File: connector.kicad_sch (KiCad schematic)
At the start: 19 parts, among them IC401 TLP185xSE, IC403 ACS71240, IC410 TLP185xSE, J400 XT60-Angled-F, Q401 HSBA8119, Q402 HSBA8119, U404 ADS1115IDGS

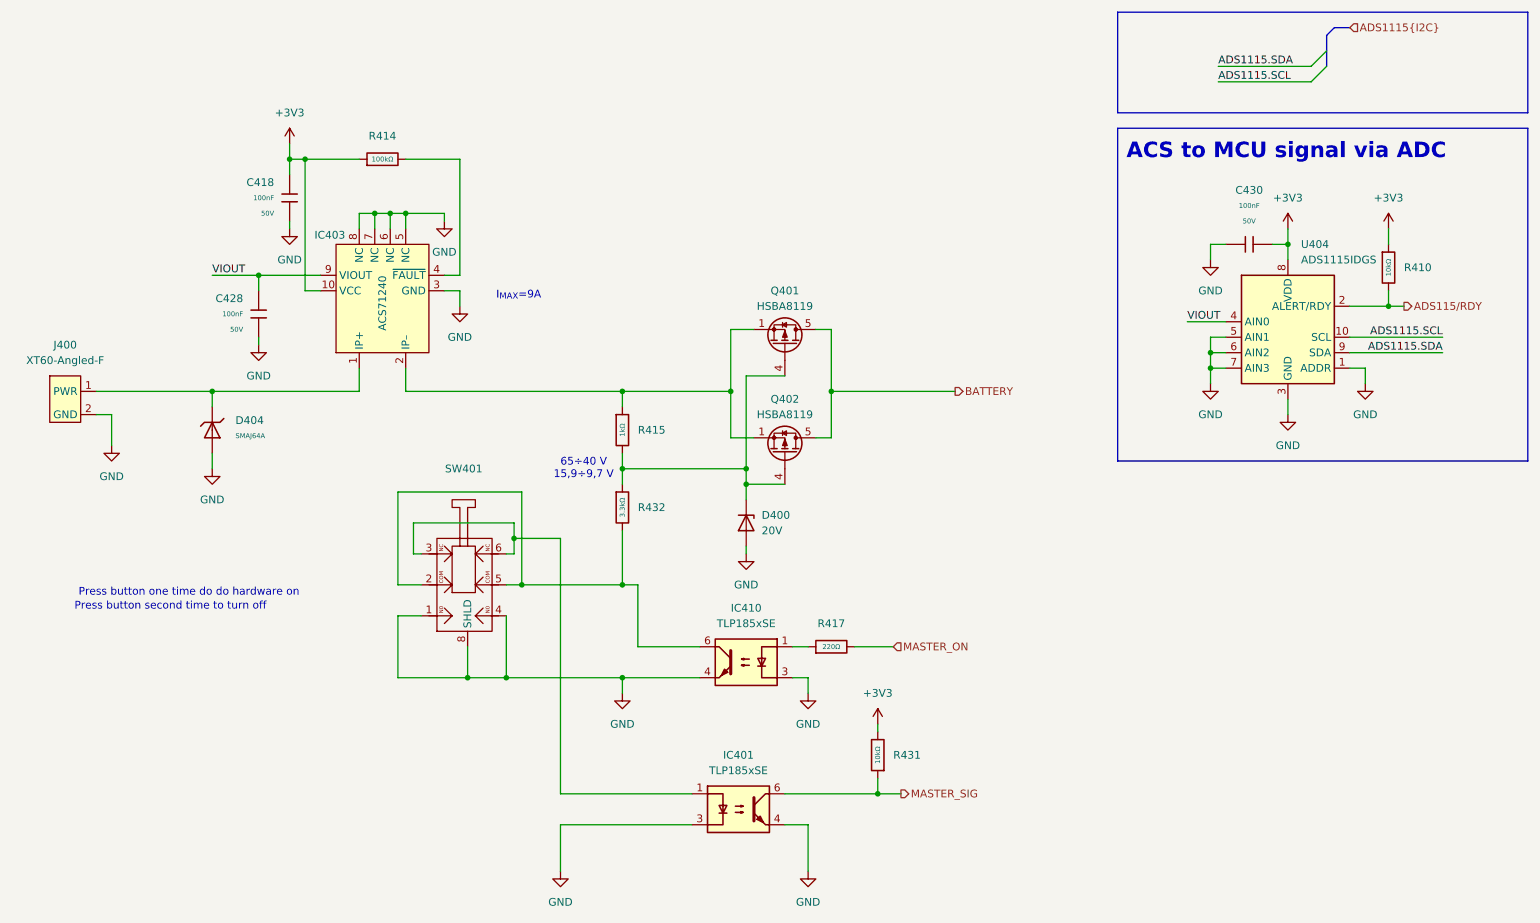
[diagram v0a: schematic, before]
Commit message: Change MCU to STM32H563
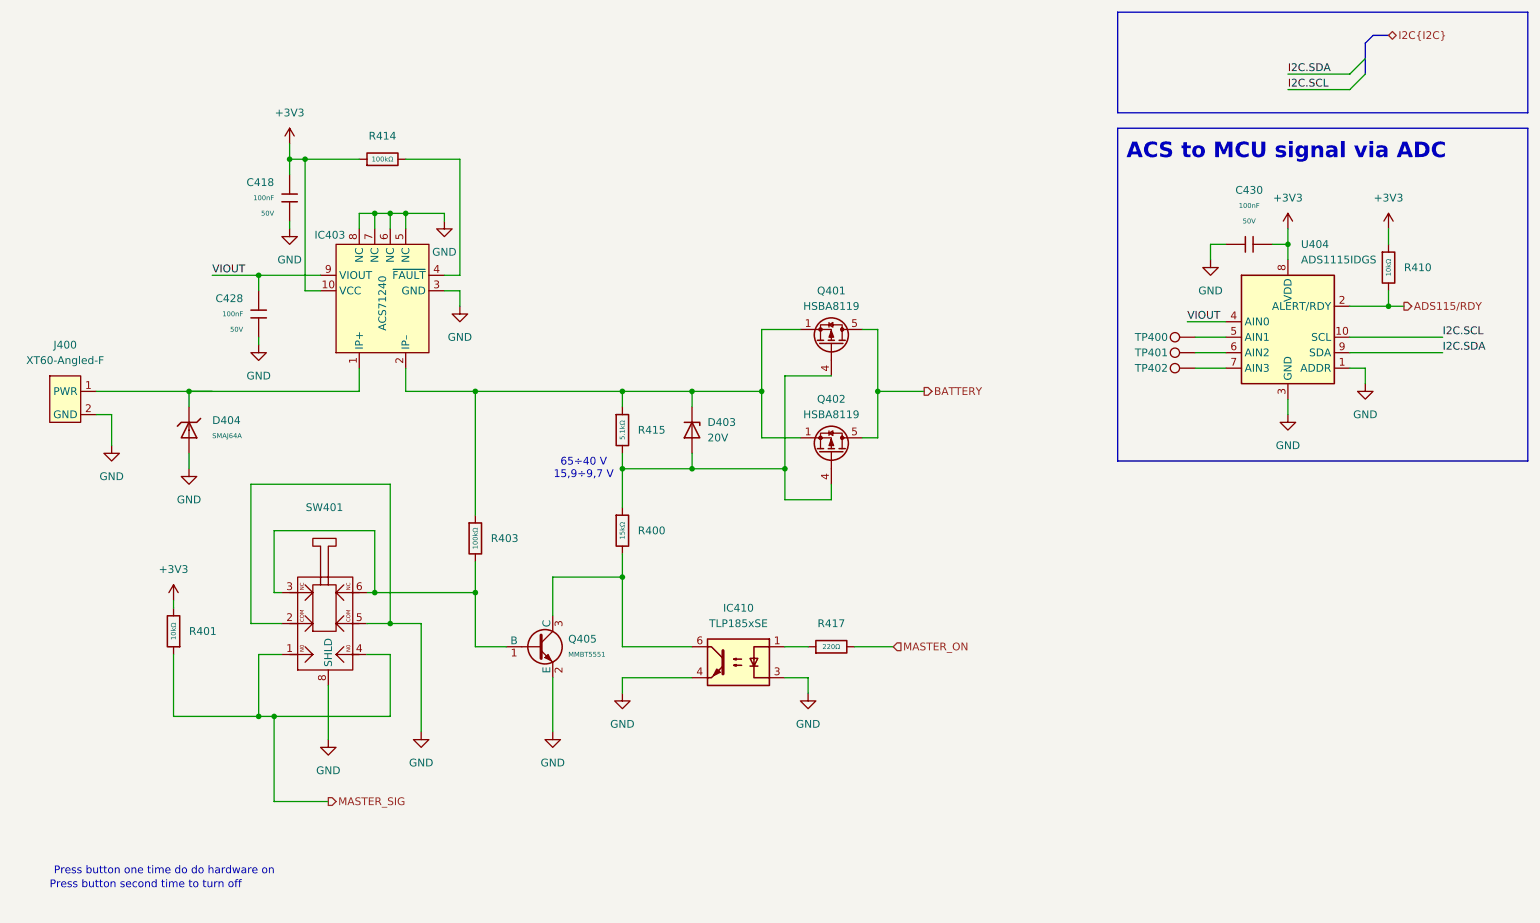
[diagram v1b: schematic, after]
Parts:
- removed D400: 20V, Diode_SMD:D_SOD-123F, symbol Device:D_Zener
- removed IC401: TLP185xSE, Package_SO:SOIC-4_4.55x3.7mm_P2.54mm, symbol Isolator:TLP185xSE
- removed R415: 1kΩ, PCM_JLCPCB:R_0603, symbol PCM_JLCPCB-Resistors:0603,1kΩ
- removed R431: 10kΩ, PCM_JLCPCB:R_0402, symbol PCM_JLCPCB-Resistors:0402,10kΩ
- removed R432: 3.3kΩ, PCM_JLCPCB:R_0603, symbol PCM_JLCPCB-Resistors:0603,3.3kΩ
- added D403: 20V, Diode_SMD:D_SOD-123F, symbol Device:D_Zener
- added Q405: MMBT5551, PCM_JLCPCB:Q_SOT-23, symbol PCM_JLCPCB-Transistors:NPN,MMBT5551
- added R400: 15kΩ, PCM_JLCPCB:R_0603, symbol PCM_JLCPCB-Resistors:0603,15kΩ
- added R401: 10kΩ, PCM_JLCPCB:R_0402, symbol PCM_JLCPCB-Resistors:0402,10kΩ
- added R403: 100kΩ, PCM_JLCPCB:R_0603, symbol PCM_JLCPCB-Resistors:0603,100kΩ
- added R415: 5.1kΩ, PCM_JLCPCB:R_0603, symbol PCM_JLCPCB-Resistors:0603,5.1kΩ
- added TP400, TP401, TP402: TestPoint, TestPoint:TestPoint_Pad_D1.0mm, symbol Connector:TestPoint
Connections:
- net +3V3: now also R401.2
- net GND: now also SW401.2 (COM), SW401.5 (COM), Q405.2 (E); no longer SW401.1 (NO), SW401.4 (NO), U404.5 (AIN1), U404.6 (AIN2), U404.7 (AIN3)
- net MASTER_SIG: now also SW401.1 (NO), SW401.4 (NO), R401.1
- net at SW401.3 (NC), SW401.6 (NC): now also Q405.1 (B), R403.2
- net at IC403.2 (IP–), Q401.1, Q401.2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: now also D403.1 (K), R403.1, R415.1
- net at Q401.4, Q402.4: now also D403.2 (A), R400.1, R415.2
- net ADS1115.SCL renamed I2C.SCL
- net ADS1115.SDA renamed I2C.SDA
- new net: TP400.1, U404.5 (AIN1)
- new net: IC410.6, Q405.3 (C), R400.2
- new net: TP402.1, U404.7 (AIN3)
- new net: TP401.1, U404.6 (AIN2)
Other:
- note removed: "I_{MAX}=9A"
- moved on the sheet: D404, IC410, Q401, Q402, SW401

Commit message: Add LCSC numbers
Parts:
- D403: LCSC (none) -> C485492
